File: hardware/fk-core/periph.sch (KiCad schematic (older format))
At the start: 9 parts, among them M1 MICROSD, P5 CONN_01X04, U5 PCF8523T, U8 FGPMMOPA6H

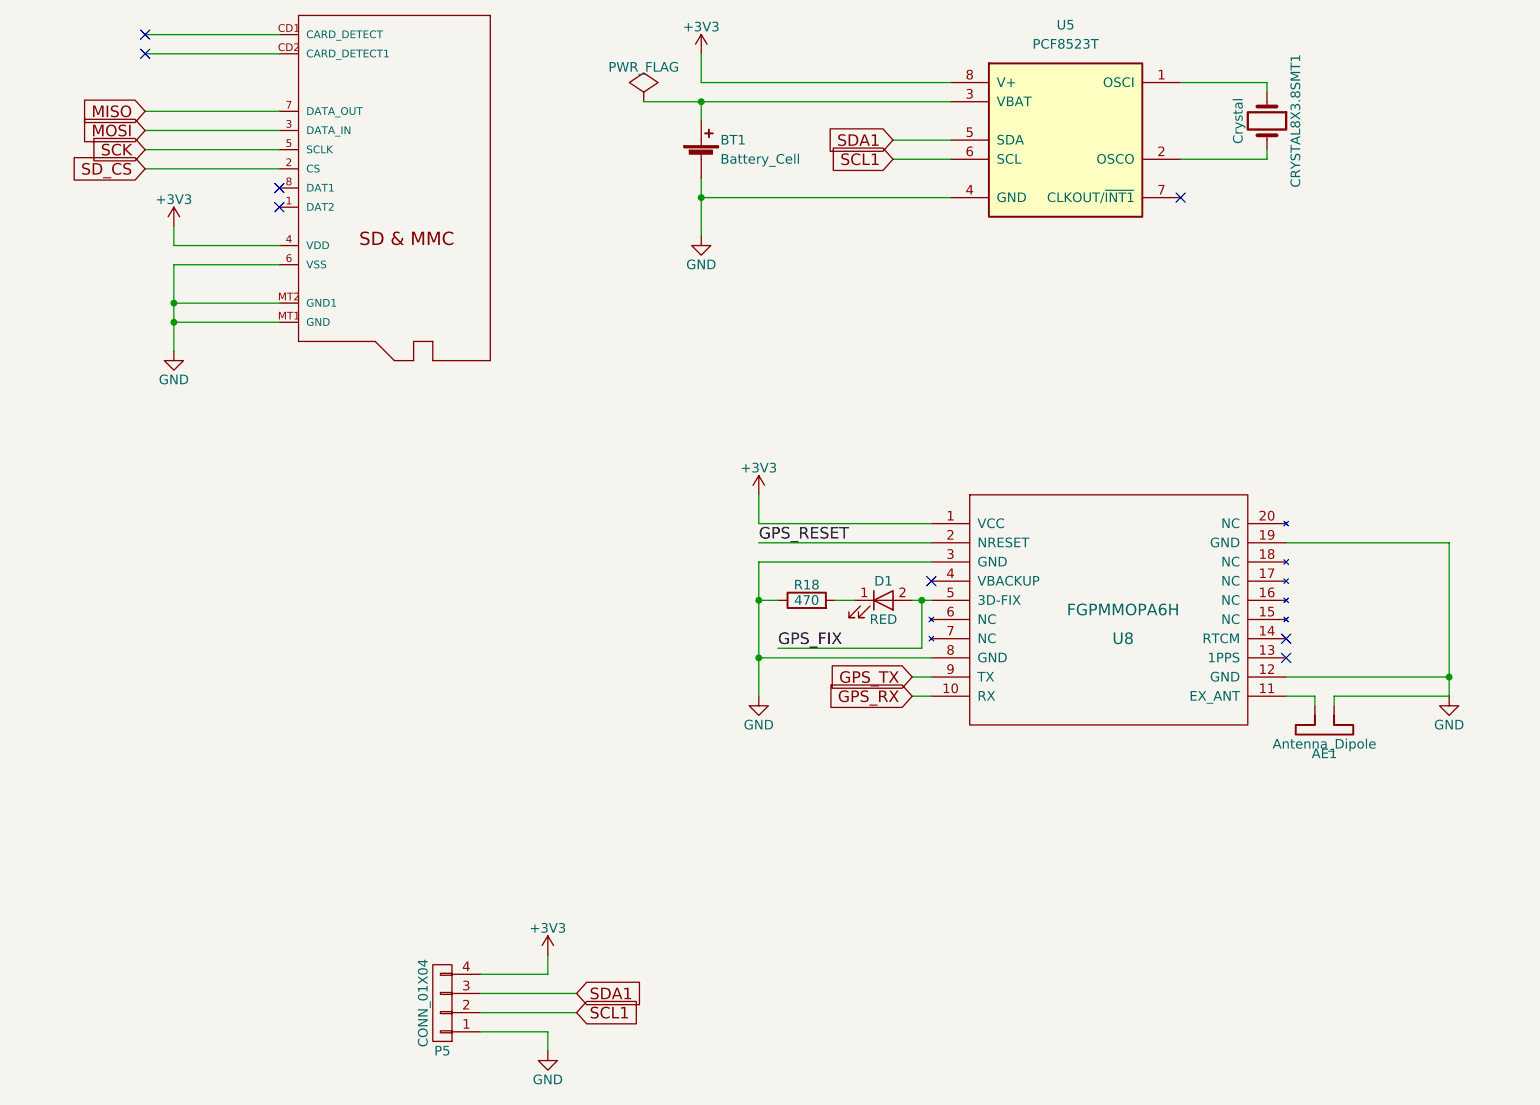
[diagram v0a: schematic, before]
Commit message: Adding better SMA connectors and the RFM95
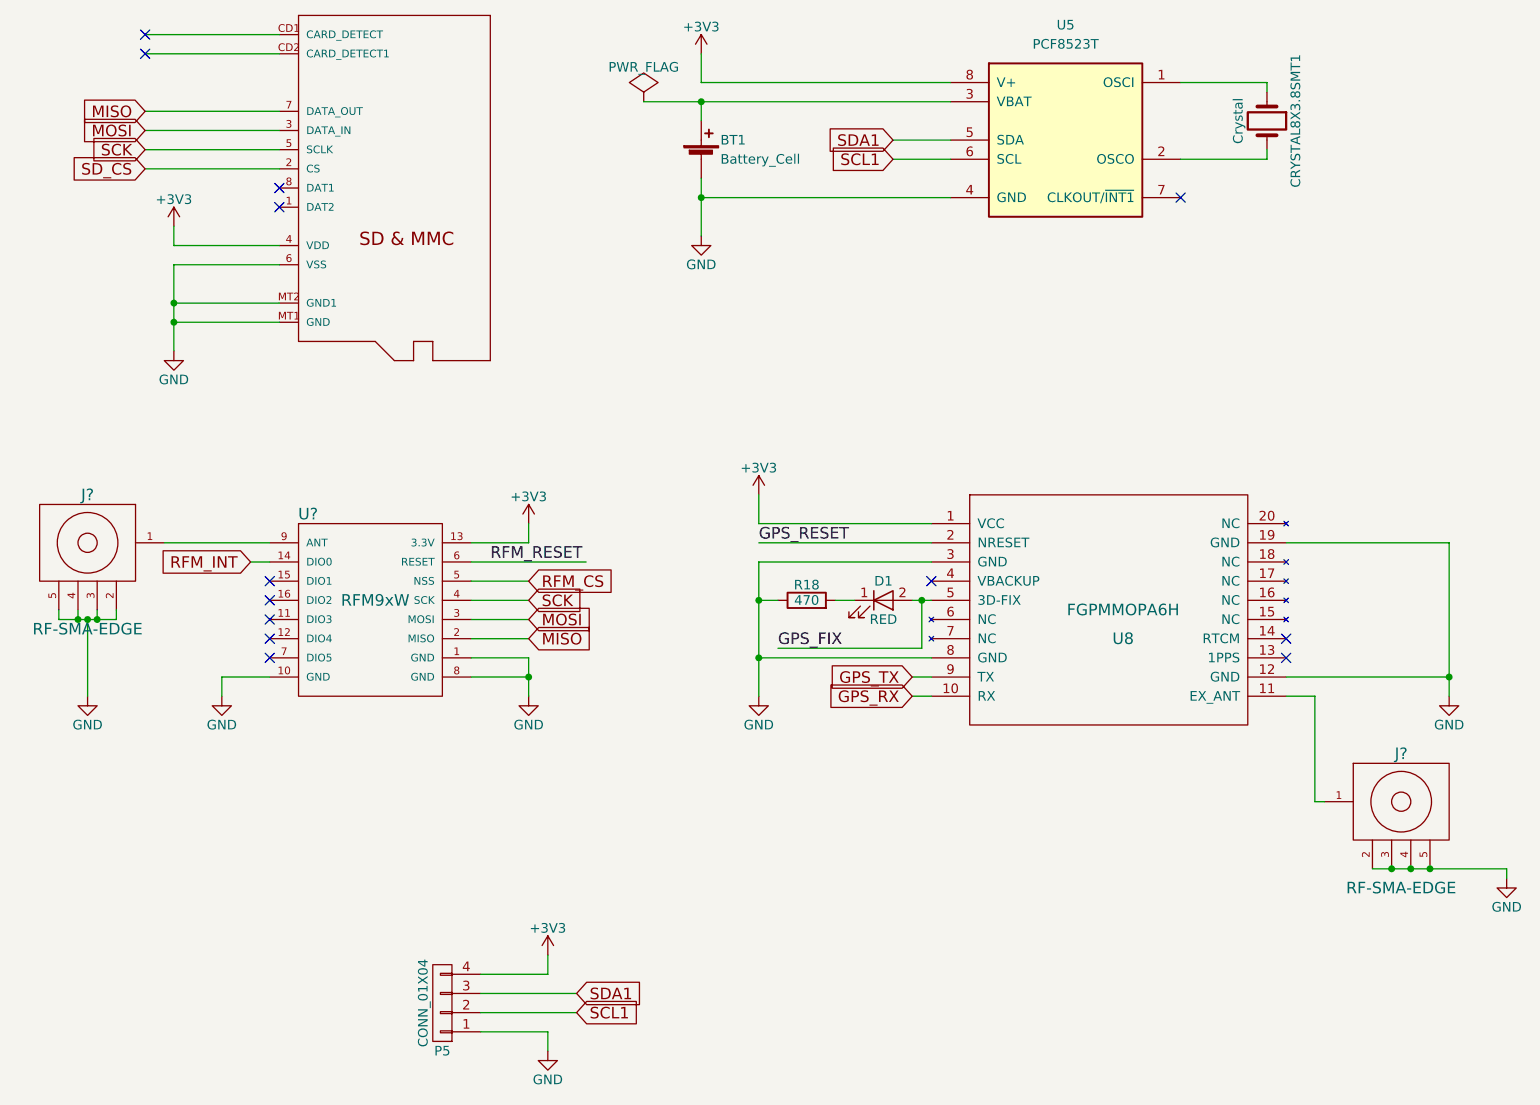
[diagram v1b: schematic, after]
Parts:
- removed AE1: Antenna_Dipole, SMA:SMA, symbol Antenna_Dipole
- added J? (x2): RF-SMA-EDGE, RocketScreamKicadLibrary:RF-SMA-EDGE, symbol RF-SMA-EDGE
- added U?: RFM9xW, RocketScreamKicadLibrary:RFM9xW, symbol RFM9xW
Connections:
- net +3V3: now also U?.13 (3.3V)
- net GND: now also J?.2, J?.2, J?.3, J?.3, J?.4, J?.4, J?.5, J?.5, U?.1 (GND), U?.10 (GND), U?.8 (GND)
- net MISO: now also U?.2 (MISO)
- net MOSI: now also U?.3 (MOSI)
- net SCK: now also U?.4 (SCK)
- net at U8.11 (EX_ANT): now also J?.1
- new net: J?.1, U?.9 (ANT)
- new net RFM_CS: U?.5 (NSS)
- new net RFM_INT: U?.14 (DIO0)
- new net RFM_RESET: U?.6 (RESET)
- no-connect marks 8 -> 13

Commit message: Some footprints, cleaning things up.
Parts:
- J1, J2: renamed from J?; footprint RocketScreamKicadLibrary:RF-SMA-EDGE -> RF-SMA-EDGE:RF-SMA-EDGE
- U10: renamed from U?; footprint RocketScreamKicadLibrary:RFM9xW -> RFM95W:RFM9xW
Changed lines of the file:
@@
 GPS_RESET
 $Comp
-L RFM9xW U?
+L RFM9xW U10
 U 1 1 588132A6
 P 3100 4500
-F 0 "U?" H 2750 5000 60  0000 C CNN
+F 0 "U10" H 2750 5000 60  0000 C CNN
 F 1 "RFM9xW" H 3100 4550 60  0000 C CNN
-F 2 "RocketScreamKicadLibrary:RFM9xW" H 3100 4000 60  0001 C CNN
+F 2 "RFM95W:RFM9xW" H 3100 4000 60  0001 C CNN
 F 3 "" H 3100 4800 60  0000 C CNN
 	1    3100 4500
@@
 $EndComp
 $Comp
-L GND #PWR?
+L GND #PWR064
 U 1 1 588134FA
 P 3900 4950
-F 0 "#PWR?" H 3900 4700 50  0001 C CNN
+F 0 "#PWR064" H 3900 4700 50  0001 C CNN
 F 1 "GND" H 3900 4800 50  0000 C CNN
 F 2 "" H 3900 4950 50  0000 C CNN
@@
 $EndComp
 $Comp
-L +3V3 #PWR?
+L +3V3 #PWR065
 U 1 1 588135AD
 P 3900 4050
-F 0 "#PWR?" H 3900 3900 50  0001 C CNN
+F 0 "#PWR065" H 3900 3900 50  0001 C CNN
 F 1 "+3V3" H 3900 4190 50  0000 C CNN
 F 2 "" H 3900 4050 50  0000 C CNN
@@
 RFM_RESET
 $Comp
-L RF-SMA-EDGE J?
+L RF-SMA-EDGE J1
 U 1 1 58813E67
 P 1600 4150
-F 0 "J?" H 1600 4400 60  0000 C CNN
+F 0 "J1" H 1600 4400 60  0000 C CNN
 F 1 "RF-SMA-EDGE" H 1600 3700 60  0000 C CNN
-F 2 "RocketScreamKicadLibrary:RF-SMA-EDGE" H 1600 3600 60  0001 C CNN
+F 2 "RF-SMA-EDGE:RF-SMA-EDGE" H 1600 3600 60  0001 C CNN
 F 3 "" H 1550 4100 60  0000 C CNN
 	1    1600 4150
@@
 	2600 2700 2050 2700
 Wire Wire Line
-	2050 2700 2050 2900
-Wire Wire Line
-	2050 2900 2050 3000
-Wire Wire Line
-	2050 3000 2050 3150
+	2050 2700 2050 3150
 Wire Wire Line
 	2600 2600 2050 2600
@@
 	5800 2050 6100 2050
 Wire Wire Line
-	4800 2250 4800 2350
-Wire Wire Line
-	4800 2350 4800 2550
+	4800 2250 4800 2550
 Wire Wire Line
 	4800 2350 6100 2350
 Wire Wire Line
-	4500 1850 4800 1850
-Wire Wire Line
-	4800 1850 6100 1850
+	4500 1850 6100 1850
 Wire Wire Line
 	4800 1850 4800 1950
@@
 	5100 4750 6000 4750
 Wire Wire Line
-	5100 4250 5100 4450
-Wire Wire Line
-	5100 4450 5100 4750
-Wire Wire Line
-	5100 4750 5100 4950
+	5100 4250 5100 4950
 Wire Wire Line
 	5100 4250 6000 4250
 Connection ~ 5100 4750
 Wire Wire Line
-	8700 4150 8700 4850
-Wire Wire Line
-	8700 4850 8700 4950
+	8700 4150 8700 4950
 Wire Wire Line
 	7850 4850 8700 4850
@@
 	5900 4850 6000 4850
 Wire Wire Line
-	5900 4450 5950 4450
-Wire Wire Line
-	5950 4450 6000 4450
+	5900 4450 6000 4450
 Wire Wire Line
 	5600 4450 5500 4450
@@
 Connection ~ 5950 4450
 Wire Wire Line
-	3900 4750 3900 4850
-Wire Wire Line
-	3900 4850 3900 4950
+	3900 4750 3900 4950
 Wire Wire Line
 	3900 4850 3600 4850
@@
 	1650 4550 1650 4500
 Wire Wire Line
-	1450 4550 1550 4550
-Wire Wire Line
-	1550 4550 1600 4550
-Wire Wire Line
-	1600 4550 1650 4550
-Wire Wire Line
-	1650 4550 1750 4550
+	1450 4550 1750 4550
 Wire Wire Line
 	1750 4550 1750 4500
@@
 Connection ~ 1600 4550
 $Comp
-L GND #PWR?
+L GND #PWR066
 U 1 1 5881447B
 P 1600 4950
-F 0 "#PWR?" H 1600 4700 50  0001 C CNN
+F 0 "#PWR066" H 1600 4700 50  0001 C CNN
 F 1 "GND" H 1600 4800 50  0000 C CNN
 F 2 "" H 1600 4950 50  0000 C CNN
@@
 $EndComp
 $Comp
-L GND #PWR?
+L GND #PWR067
 U 1 1 5881451F
 P 2300 4950
-F 0 "#PWR?" H 2300 4700 50  0001 C CNN
+F 0 "#PWR067" H 2300 4700 50  0001 C CNN
 F 1 "GND" H 2300 4800 50  0000 C CNN
 F 2 "" H 2300 4950 50  0000 C CNN
@@
 	2000 4150 2550 4150
 $Comp
-L RF-SMA-EDGE J?
+L RF-SMA-EDGE J2
 U 1 1 58814EB3
 P 8450 5500
-F 0 "J?" H 8450 5750 60  0000 C CNN
+F 0 "J2" H 8450 5750 60  0000 C CNN
 F 1 "RF-SMA-EDGE" H 8450 5050 60  0000 C CNN
-F 2 "RocketScreamKicadLibrary:RF-SMA-EDGE" H 8450 4950 60  0001 C CNN
+F 2 "RF-SMA-EDGE:RF-SMA-EDGE" H 8450 4950 60  0001 C CNN
 F 3 "" H 8400 5450 60  0000 C CNN
 	1    8450 5500
@@
 	8000 5500 8050 5500
 $Comp
-L GND #PWR?
+L GND #PWR068
 U 1 1 5881536E
 P 9000 5900
-F 0 "#PWR?" H 9000 5650 50  0001 C CNN
+F 0 "#PWR068" H 9000 5650 50  0001 C CNN
 F 1 "GND" H 9000 5750 50  0000 C CNN
 F 2 "" H 9000 5900 50  0000 C CNN
@@
 $EndComp
 Wire Wire Line
-	8300 5850 8400 5850
-Wire Wire Line
-	8400 5850 8500 5850
-Wire Wire Line
-	8500 5850 8600 5850
-Wire Wire Line
-	8600 5850 9000 5850
+	8300 5850 9000 5850
 Connection ~ 8400 5850
 Connection ~ 8500 5850
